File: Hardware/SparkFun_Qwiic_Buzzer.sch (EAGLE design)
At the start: 43 parts, among them J2 QWIIC_RA, J3 QWIIC_RA, Q3 200mA/40V, U4 ATTINY84-ARDUINO

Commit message: Layout done
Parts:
- removed LOGO3: SFE_LOGO_NAME.1_INCH, SparkFun-Aesthetics:SFE_LOGO_NAME.1_INCH
- added LOGO2: SFE_LOGO_NAME_FLAME.1_INCH, SparkFun-Aesthetics:SFE_LOGO_NAME_FLAME.1_INCH
- added R9: USER, SparkFun-Resistors:RESISTORAXIAL-0.3
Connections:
- removed net STAT: U4.(A3)3
- net N$15: now also R9.1
- net N$4: now also R9.2
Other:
- note added: "Cut jumper to disconnect LED."
- moved on the sheet: Q1G1, Q1G2, Q2G1, Q2G2

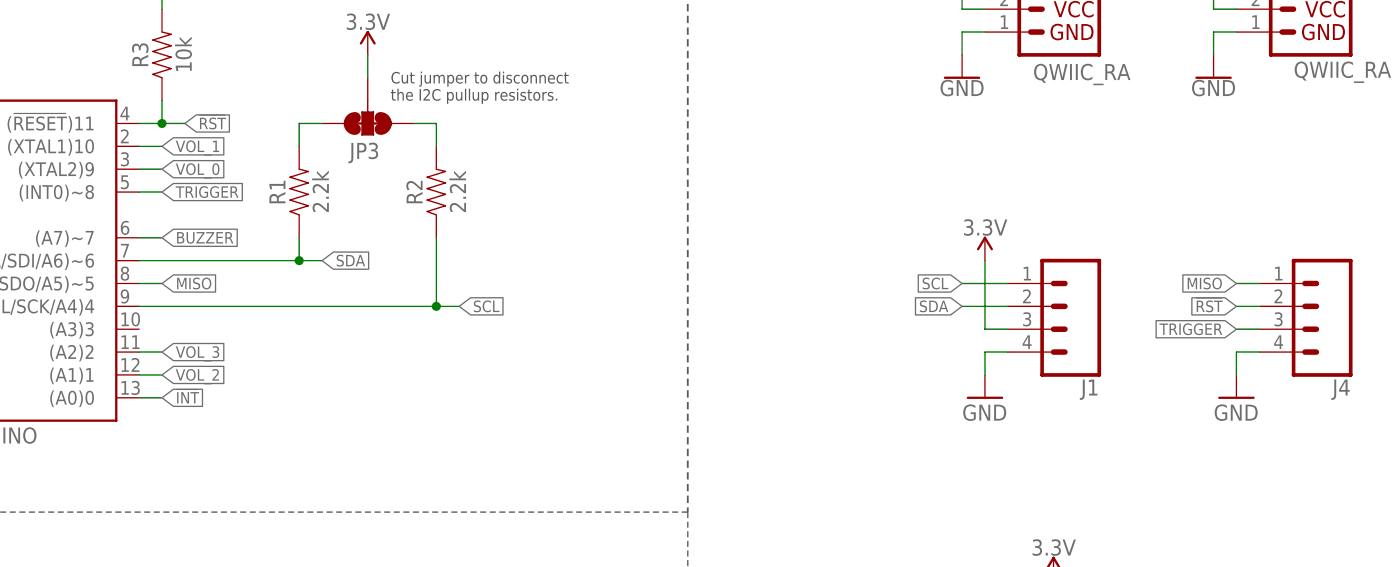
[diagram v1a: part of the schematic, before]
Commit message: updated miso to poci
both net names and board header silk
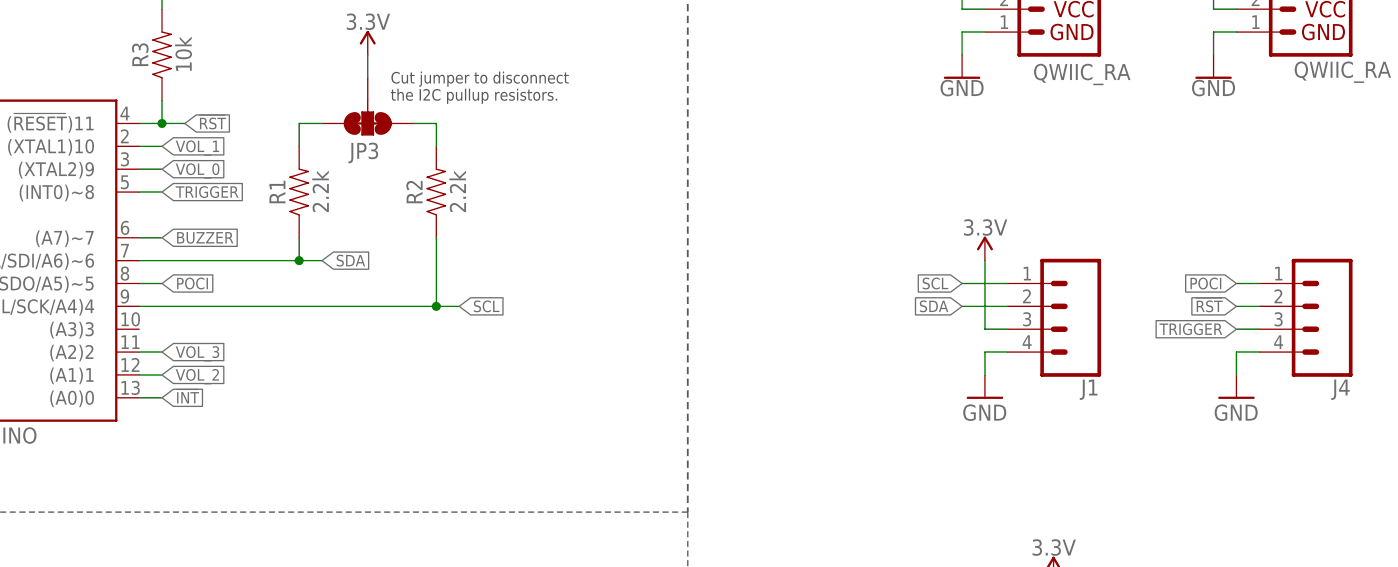
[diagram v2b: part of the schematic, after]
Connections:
- net MISO renamed POCI
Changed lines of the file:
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@@
 </segment>
 </net>
-<net name="MISO" class="0">
+<net name="POCI" class="0">
 <segment>
 <pinref part="U4" gate="U1" pin="(TX/\SDO/A5)~5"/>

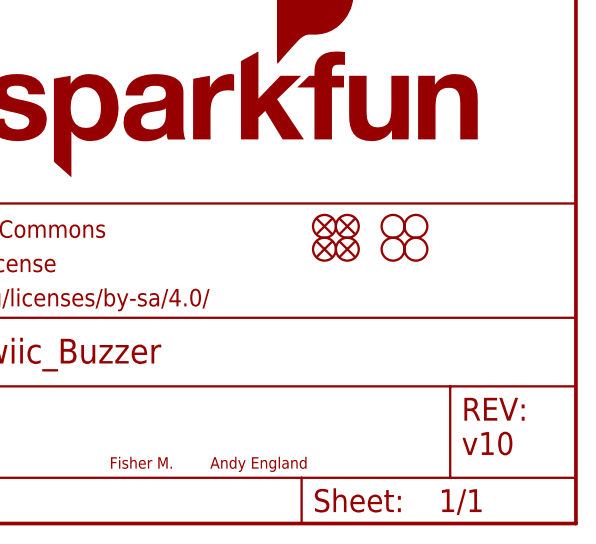
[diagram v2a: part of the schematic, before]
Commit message: add ordering instructions
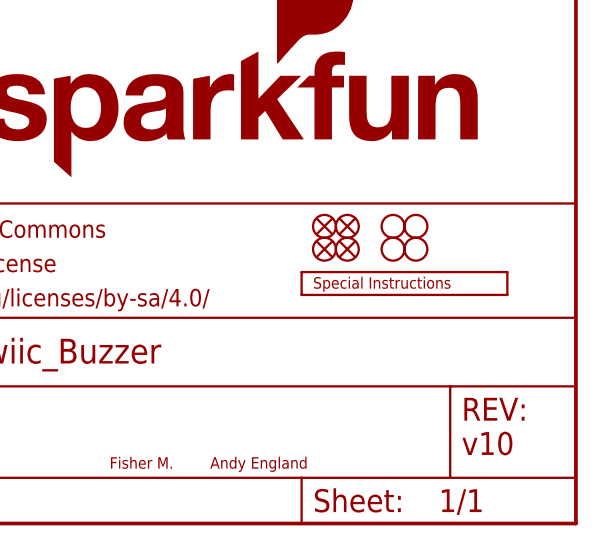
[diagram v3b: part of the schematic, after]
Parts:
- added LOGO3: SPECIAL_INSTRUCTIONS-ORDERING, SparkFun-Aesthetics:SPECIAL_INSTRUCTIONS-ORDERING
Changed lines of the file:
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@@
 <part name="R9" library="SparkFun-Resistors" deviceset="RESISTOR" device="AXIAL-0.3" value="USER"/>
 <part name="LOGO2" library="SparkFun-Aesthetics" deviceset="SFE_LOGO_NAME_FLAME" device=".1_INCH"/>
+<part name="LOGO3" library="SparkFun-Aesthetics" deviceset="SPECIAL_INSTRUCTIONS" device="-ORDERING"/>
 </parts>
 <sheets>
@@
 </instance>
 <instance part="LOGO2" gate="G$1" x="182.88" y="38.1" smashed="yes"/>
+<instance part="LOGO3" gate="G$1" x="218.44" y="25.4" smashed="yes"/>
 </instances>
 <busses>
